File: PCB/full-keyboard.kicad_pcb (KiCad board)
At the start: 2 copper layers, 332 parts, among them J1 Conn_01x04_Pin, SW1 SW_Push, SW10 SW_Push, SW100 SW_Push, SW101 SW_Push, SW102 SW_Push, SW103 SW_Push, SW104 SW_Push, SW105 SW_Push, SW106 SW_Push, SW107 SW_Push, SW108 SW_Push, SW109 RotaryEncoder_Switch, SW11 SW_Push, SW110 RotaryEncoder_Switch, SW12 SW_Push, SW13 SW_Push, SW14 SW_Push, SW15 SW_Push, SW16 SW_Push, SW17 SW_Push, SW18 SW_Push, SW19 SW_Push, SW2 SW_Push, SW20 SW_Push, SW21 SW_Push, SW22 SW_Push, SW23 SW_Push, SW24 SW_Push, SW25 SW_Push, SW26 SW_Push, SW27 SW_Push, SW28 SW_Push, SW29 SW_Push, SW3 SW_Push, SW30 SW_Push, SW31 SW_Push, SW32 SW_Push, SW33 SW_Push, SW34 SW_Push, SW35 SW_Push, SW36 SW_Push, SW37 SW_Push, SW38 SW_Push, SW39 SW_Push, SW4 SW_Push, SW40 SW_Push, SW41 SW_Push, SW42 SW_Push, SW43 SW_Push, SW44 SW_Push, SW45 SW_Push, SW46 SW_Push, SW47 SW_Push, SW48 SW_Push, SW49 SW_Push, SW5 SW_Push, SW50 SW_Push, SW51 SW_Push, SW52 SW_Push, SW53 SW_Push, SW54 SW_Push, SW55 SW_Push, SW56 SW_Push, SW57 SW_Push, SW58 SW_Push, SW59 SW_Push, SW6 SW_Push, SW60 SW_Push, SW61 SW_Push, SW62 SW_Push, SW63 SW_Push, SW64 SW_Push, SW65 SW_Push, SW66 SW_Push, SW67 SW_Push, SW68 SW_Push, SW69 SW_Push, SW7 SW_Push, SW70 SW_Push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

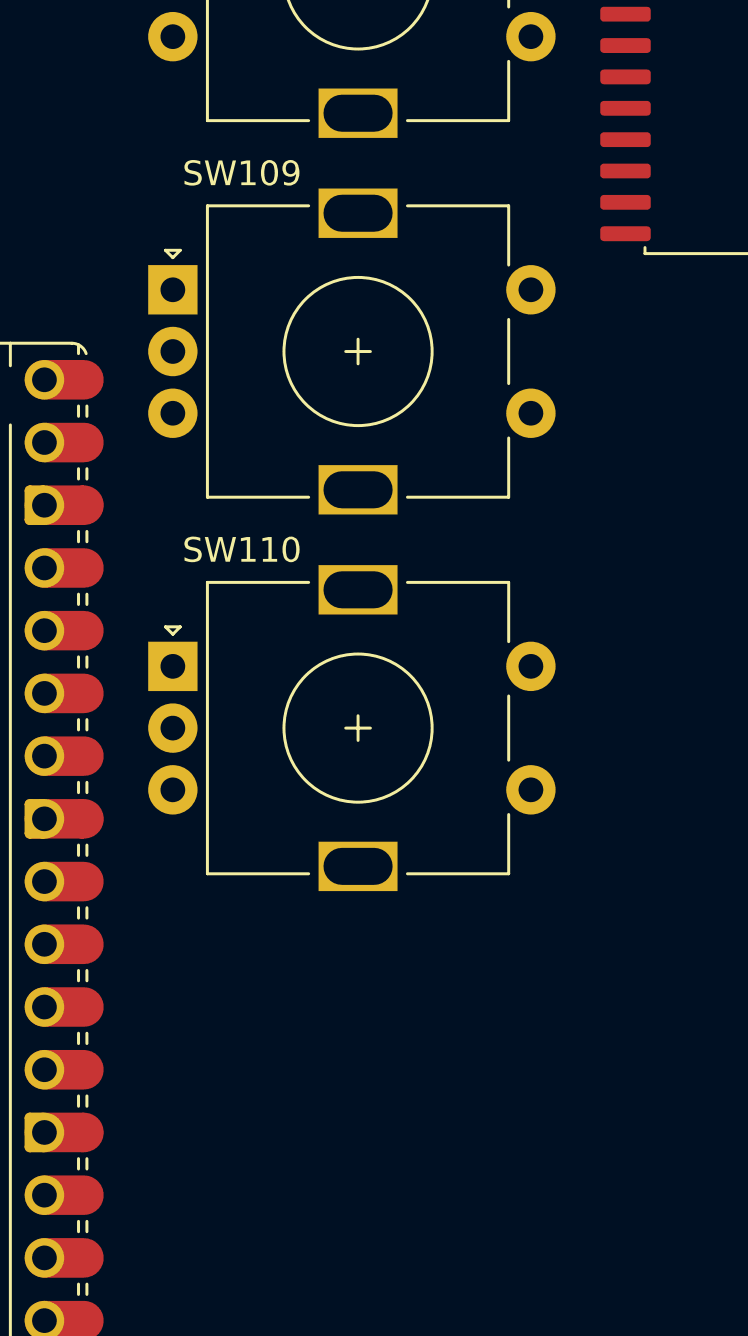
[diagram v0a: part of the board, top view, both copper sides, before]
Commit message: updated some footprints and found a cheaper hotswap socket kit
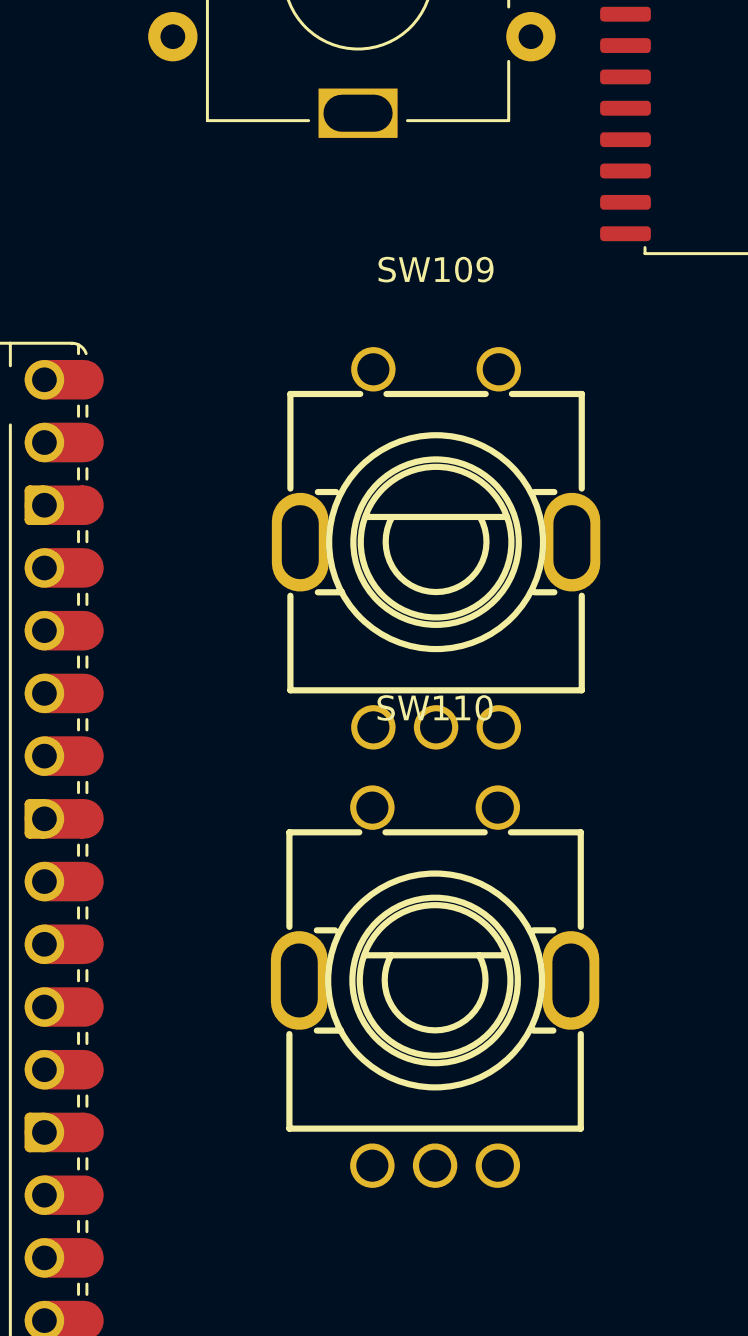
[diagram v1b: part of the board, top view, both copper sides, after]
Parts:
- SW109, SW110: footprint Rotary_Encoder:RotaryEncoder_Alps_EC11E-Switch_Vertical_H20mm -> easyeda2kicad:SW-TH_EC11XXXXXXXX
- moved SW110 16.8 mm to (504.5, 187.5)
- moved SW109 14.9 mm to (504.5, 169.8)

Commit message: worked on laying out the keyboard
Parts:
- R1, R2, R3: footprint easyeda2kicad:RES-TH_BD2.5-L4.7-P8.70-D0.5 -> Resistor_THT:R_Axial_DIN0207_L6.3mm_D2.5mm_P2.54mm_Vertical
- U1: footprint Package_SO:SOIC-28W_7.5x17.9mm_P1.27mm -> Package_DIP:DIP-28_W7.62mm
- moved SW1 272.0 mm to (46.6, 63.5)
- moved SW2 233.5 mm to (85.6, 63.5)
- moved SW3 215.5 mm to (105.6, 63.5)
- moved SW4 200.0 mm to (125.1, 63.5)
- moved SW104 190.8 mm to (525.8, 345.6)
- moved SW12 190.8 mm to (385.4, 433.4)
- moved SW19 190.8 mm to (402.9, 345.6)
- moved SW24 190.8 mm to (402.9, 433.4)
- moved SW31 190.8 mm to (420.5, 345.6)
- moved SW36 190.8 mm to (420.5, 433.4)
- moved SW43 190.8 mm to (438.0, 345.6)
- moved SW48 190.8 mm to (438.0, 433.4)
- moved SW55 190.8 mm to (455.6, 345.6)
- moved SW60 190.8 mm to (455.6, 433.4)
- moved SW67 190.8 mm to (473.1, 345.6)
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
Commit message: started laying out the pcb
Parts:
- moved SW12 379.5 mm to (302.0, 63.1)
- moved SW11 366.5 mm to (282.6, 64.0)
- moved SW10 356.4 mm to (263.1, 63.5)
- moved SW9 351.6 mm to (233.5, 63.6)
- moved SW8 345.1 mm to (214.0, 63.6)
- moved SW18 265.9 mm to (431.0, 63.6)
- moved SW17 247.1 mm to (411.1, 63.5)
- moved SW16 229.9 mm to (387.0, 63.6)
- moved SW15 214.9 mm to (367.0, 63.5)
- moved SW14 202.6 mm to (347.0, 63.1)
- moved SW13 194.1 mm to (322.5, 63.6)
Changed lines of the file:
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@@
 	(footprint "key-switches:SW_MX_Kailh_Choc_V1V2_THT_Hybrid"
 		(layer "F.Cu")
-		(at 385.38 363.15)
+		(at 214 63.65)
 		(descr "Compatible with Cherry MX, Kailh Choc V1 (PG1350) and Choc V2 (PG1353) mechanical keyboard switch, through-hole soldering, single-sided mounting.")
 		(tags "switch, low_profile")
@@
 	(footprint "key-switches:SW_MX_Kailh_Choc_V1V2_THT_Hybrid"
 		(layer "F.Cu")
-		(at 385.38 433.35)
+		(at 302 63.15)
 		(descr "Compatible with Cherry MX, Kailh Choc V1 (PG1350) and Choc V2 (PG1353) mechanical keyboard switch, through-hole soldering, single-sided mounting.")
 		(tags "switch, low_profile")
@@
 	(footprint "key-switches:SW_MX_Kailh_Choc_V1V2_THT_Hybrid"
 		(layer "F.Cu")
-		(at 385.38 415.8)
+		(at 282.58 64)
 		(descr "Compatible with Cherry MX, Kailh Choc V1 (PG1350) and Choc V2 (PG1353) mechanical keyboard switch, through-hole soldering, single-sided mounting.")
 		(tags "switch, low_profile")
@@
 	(footprint "key-switches:SW_MX_Kailh_Choc_V1V2_THT_Hybrid"
 		(layer "F.Cu")
-		(at 402.93 328.05)
+		(at 431 63.65)
 		(descr "Compatible with Cherry MX, Kailh Choc V1 (PG1350) and Choc V2 (PG1353) mechanical keyboard switch, through-hole soldering, single-sided mounting.")
 		(tags "switch, low_profile")
@@
 	(footprint "key-switches:SW_MX_Kailh_Choc_V1V2_THT_Hybrid"
 		(layer "F.Cu")
-		(at 402.93 257.85)
+		(at 347 63.15)
 		(descr "Compatible with Cherry MX, Kailh Choc V1 (PG1350) and Choc V2 (PG1353) mechanical keyboard switch, through-hole soldering, single-sided mounting.")
 		(tags "switch, low_profile")
@@
 	(footprint "key-switches:SW_MX_Kailh_Choc_V1V2_THT_Hybrid"
 		(layer "F.Cu")
-		(at 385.38 398.25)
+		(at 263.08 63.5)
 		(descr "Compatible with Cherry MX, Kailh Choc V1 (PG1350) and Choc V2 (PG1353) mechanical keyboard switch, through-hole soldering, single-sided mounting.")
 		(tags "switch, low_profile")
@@
 	(footprint "key-switches:SW_MX_Kailh_Choc_V1V2_THT_Hybrid"
 		(layer "F.Cu")
-		(at 385.38 380.7)
+		(at 233.5 63.65)
 		(descr "Compatible with Cherry MX, Kailh Choc V1 (PG1350) and Choc V2 (PG1353) mechanical keyboard switch, through-hole soldering, single-sided mounting.")
 		(tags "switch, low_profile")
@@
 	(footprint "key-switches:SW_MX_Kailh_Choc_V1V2_THT_Hybrid"
 		(layer "F.Cu")
-		(at 402.93 310.5)
+		(at 411.08 63.5)
 		(descr "Compatible with Cherry MX, Kailh Choc V1 (PG1350) and Choc V2 (PG1353) mechanical keyboard switch, through-hole soldering, single-sided mounting.")
 		(tags "switch, low_profile")
@@
 	(footprint "key-switches:SW_MX_Kailh_Choc_V1V2_THT_Hybrid"
 		(layer "F.Cu")
-		(at 402.93 240.3)
+		(at 322.5 63.65)
 		(descr "Compatible with Cherry MX, Kailh Choc V1 (PG1350) and Choc V2 (PG1353) mechanical keyboard switch, through-hole soldering, single-sided mounting.")
 		(tags "switch, low_profile")
@@
 	(footprint "key-switches:SW_MX_Kailh_Choc_V1V2_THT_Hybrid"
 		(layer "F.Cu")
-		(at 402.93 275.4)
+		(at 367 63.5)
 		(descr "Compatible with Cherry MX, Kailh Choc V1 (PG1350) and Choc V2 (PG1353) mechanical keyboard switch, through-hole soldering, single-sided mounting.")
 		(tags "switch, low_profile")
@@
 	(footprint "key-switches:SW_MX_Kailh_Choc_V1V2_THT_Hybrid"
 		(layer "F.Cu")
-		(at 402.93 292.95)
+		(at 387 63.65)
 		(descr "Compatible with Cherry MX, Kailh Choc V1 (PG1350) and Choc V2 (PG1353) mechanical keyboard switch, through-hole soldering, single-sided mounting.")
 		(tags "switch, low_profile")

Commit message: set the layout in the schematic to match the pcb layout for the keys
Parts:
- removed SW110: RotaryEncoder_Switch, easyeda2kicad:SW-TH_EC11XXXXXXXX
- SW95: footprint Rotary_Encoder:RotaryEncoder_Alps_EC11E-Switch_Vertical_H20mm -> key-switches:SW_MX_Kailh_Choc_V1V2_THT_Hybrid
- moved SW96 520.6 mm to (48.5, 171.5)
- moved SW97 506.8 mm to (74.0, 172.0)
- moved SW79 472.6 mm to (59.6, 152.0)
- moved SW21 458.1 mm to (46.5, 93.0)
- moved SW22 454.2 mm to (66.6, 93.0)
- moved SW23 452.7 mm to (85.6, 93.0)
- moved SW80 452.0 mm to (91.0, 152.2)
- moved SW24 451.9 mm to (105.6, 93.0)
- moved SW81 443.6 mm to (110.6, 152.0)
- moved SW63 442.8 mm to (54.0, 132.5)
- moved SW42 442.3 mm to (51.6, 113.0)
- moved SW82 436.7 mm to (130.1, 152.0)
- moved SW83 431.5 mm to (149.5, 151.7)
- moved SW98 431.3 mm to (100.0, 171.5)
- moved SW43 430.5 mm to (76.0, 112.7)
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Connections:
- D1 pad 1: /ROW0 -> unconnected-(D1-K-Pad1)
- D10 pad 1: /ROW0 -> unconnected-(D10-K-Pad1)
- D100 pad 1: /ROW5 -> unconnected-(D100-K-Pad1)
- D101 pad 1: /ROW5 -> unconnected-(D101-K-Pad1)
- D102 pad 1: /ROW5 -> unconnected-(D102-K-Pad1)
- D103 pad 1: /ROW5 -> unconnected-(D103-K-Pad1)
- D104 pad 1: /ROW5 -> unconnected-(D104-K-Pad1)
- D105 pad 1: /ROW5 -> unconnected-(D105-K-Pad1)
- D106 pad 1: /ROW5 -> unconnected-(D106-K-Pad1)
- D107 pad 1: /ROW5 -> unconnected-(D107-K-Pad1)
- D108 pad 1: /ROW5 -> unconnected-(D108-K-Pad1)
- D11 pad 1: /ROW0 -> unconnected-(D11-K-Pad1)
- D12 pad 1: /ROW0 -> unconnected-(D12-K-Pad1)
- D13 pad 1: /ROW0 -> unconnected-(D13-K-Pad1)
- D14 pad 1: /ROW0 -> unconnected-(D14-K-Pad1)
- D15 pad 1: /ROW0 -> unconnected-(D15-K-Pad1)
- D16 pad 1: /ROW0 -> unconnected-(D16-K-Pad1)
- D17 pad 1: /ROW0 -> unconnected-(D17-K-Pad1)
- D18 pad 1: /ROW0 -> unconnected-(D18-K-Pad1)
- D19 pad 1: /ROW1 -> unconnected-(D19-K-Pad1)
- D2 pad 1: /ROW0 -> unconnected-(D2-K-Pad1)
- D20 pad 1: /ROW1 -> unconnected-(D20-K-Pad1)
- D21 pad 1: /ROW1 -> unconnected-(D21-K-Pad1)
- D22 pad 1: /ROW1 -> unconnected-(D22-K-Pad1)
- D23 pad 1: /ROW1 -> unconnected-(D23-K-Pad1)
- D24 pad 1: /ROW1 -> unconnected-(D24-K-Pad1)
- D25 pad 1: /ROW1 -> unconnected-(D25-K-Pad1)
- D26 pad 1: /ROW1 -> unconnected-(D26-K-Pad1)
- D27 pad 1: /ROW1 -> unconnected-(D27-K-Pad1)
- D28 pad 1: /ROW1 -> unconnected-(D28-K-Pad1)
- D29 pad 1: /ROW1 -> unconnected-(D29-K-Pad1)
- D3 pad 1: /ROW0 -> unconnected-(D3-K-Pad1)
- D30 pad 1: /ROW1 -> unconnected-(D30-K-Pad1)
- D31 pad 1: /ROW1 -> unconnected-(D31-K-Pad1)
- D32 pad 1: /ROW1 -> unconnected-(D32-K-Pad1)
- D33 pad 1: /ROW1 -> unconnected-(D33-K-Pad1)
- D34 pad 1: /ROW1 -> unconnected-(D34-K-Pad1)
- D35 pad 1: /ROW1 -> unconnected-(D35-K-Pad1)
- D36 pad 1: /ROW1 -> unconnected-(D36-K-Pad1)
- D37 pad 1: /ROW2 -> unconnected-(D37-K-Pad1)
- D38 pad 1: /ROW2 -> unconnected-(D38-K-Pad1)
- D39 pad 1: /ROW2 -> unconnected-(D39-K-Pad1)
- D4 pad 1: /ROW0 -> unconnected-(D4-K-Pad1)
- D40 pad 1: /ROW2 -> unconnected-(D40-K-Pad1)
- D41 pad 1: /ROW2 -> unconnected-(D41-K-Pad1)
- D42 pad 1: /ROW2 -> unconnected-(D42-K-Pad1)
- D43 pad 1: /ROW2 -> unconnected-(D43-K-Pad1)
- D44 pad 1: /ROW2 -> unconnected-(D44-K-Pad1)
- D45 pad 1: /ROW2 -> unconnected-(D45-K-Pad1)
- D46 pad 1: /ROW2 -> unconnected-(D46-K-Pad1)
- D47 pad 1: /ROW2 -> unconnected-(D47-K-Pad1)
- D48 pad 1: /ROW2 -> unconnected-(D48-K-Pad1)
- D49 pad 1: /ROW2 -> unconnected-(D49-K-Pad1)
- D5 pad 1: /ROW0 -> unconnected-(D5-K-Pad1)
- D50 pad 1: /ROW2 -> unconnected-(D50-K-Pad1)
- D51 pad 1: /ROW2 -> unconnected-(D51-K-Pad1)
- D52 pad 1: /ROW2 -> unconnected-(D52-K-Pad1)
- D53 pad 1: /ROW2 -> unconnected-(D53-K-Pad1)
- D54 pad 1: /ROW2 -> unconnected-(D54-K-Pad1)
- D55 pad 1: /ROW3 -> unconnected-(D55-K-Pad1)
- D56 pad 1: /ROW3 -> unconnected-(D56-K-Pad1)
- D57 pad 1: /ROW3 -> unconnected-(D57-K-Pad1)
- D58 pad 1: /ROW3 -> unconnected-(D58-K-Pad1)
- D59 pad 1: /ROW3 -> unconnected-(D59-K-Pad1)
- D6 pad 1: /ROW0 -> unconnected-(D6-K-Pad1)
- D60 pad 1: /ROW3 -> unconnected-(D60-K-Pad1)
- D61 pad 1: /ROW3 -> unconnected-(D61-K-Pad1)
- D62 pad 1: /ROW3 -> unconnected-(D62-K-Pad1)
- D63 pad 1: /ROW3 -> unconnected-(D63-K-Pad1)
- D64 pad 1: /ROW3 -> unconnected-(D64-K-Pad1)
- D65 pad 1: /ROW3 -> unconnected-(D65-K-Pad1)
- D66 pad 1: /ROW3 -> unconnected-(D66-K-Pad1)
- D67 pad 1: /ROW3 -> unconnected-(D67-K-Pad1)
- D68 pad 1: /ROW3 -> unconnected-(D68-K-Pad1)
- D69 pad 1: /ROW3 -> unconnected-(D69-K-Pad1)
- D7 pad 1: /ROW0 -> unconnected-(D7-K-Pad1)
- D70 pad 1: /ROW3 -> unconnected-(D70-K-Pad1)
- D71 pad 1: /ROW3 -> unconnected-(D71-K-Pad1)
- D72 pad 1: /ROW3 -> unconnected-(D72-K-Pad1)
- D73 pad 1: /ROW4 -> unconnected-(D73-K-Pad1)
- D74 pad 1: /ROW4 -> unconnected-(D74-K-Pad1)
- D75 pad 1: /ROW4 -> unconnected-(D75-K-Pad1)
- D76 pad 1: /ROW4 -> unconnected-(D76-K-Pad1)
- D77 pad 1: /ROW4 -> unconnected-(D77-K-Pad1)
- D78 pad 1: /ROW4 -> unconnected-(D78-K-Pad1)
- D79 pad 1: /ROW4 -> unconnected-(D79-K-Pad1)
- D8 pad 1: /ROW0 -> unconnected-(D8-K-Pad1)
- D80 pad 1: /ROW4 -> unconnected-(D80-K-Pad1)
- D81 pad 1: /ROW4 -> unconnected-(D81-K-Pad1)
- D82 pad 1: /ROW4 -> unconnected-(D82-K-Pad1)
- D83 pad 1: /ROW4 -> unconnected-(D83-K-Pad1)
- D84 pad 1: /ROW4 -> unconnected-(D84-K-Pad1)
- D85 pad 1: /ROW4 -> unconnected-(D85-K-Pad1)
- D86 pad 1: /ROW4 -> unconnected-(D86-K-Pad1)
- D87 pad 1: /ROW4 -> unconnected-(D87-K-Pad1)
- D88 pad 1: /ROW4 -> unconnected-(D88-K-Pad1)
- D89 pad 1: /ROW4 -> unconnected-(D89-K-Pad1)
- D9 pad 1: /ROW0 -> unconnected-(D9-K-Pad1)
- D90 pad 1: /ROW4 -> unconnected-(D90-K-Pad1)
- D91 pad 1: /ROW5 -> unconnected-(D91-K-Pad1)
- D92 pad 1: /ROW5 -> unconnected-(D92-K-Pad1)
- D93 pad 1: /ROW5 -> unconnected-(D93-K-Pad1)
- D94 pad 1: /ROW5 -> unconnected-(D94-K-Pad1)
- D95 pad 1: /ROW5 -> unconnected-(D95-K-Pad1)
- D96 pad 1: /ROW5 -> unconnected-(D96-K-Pad1)
- D97 pad 1: /ROW5 -> unconnected-(D97-K-Pad1)
- D98 pad 1: /ROW5 -> unconnected-(D98-K-Pad1)
- D99 pad 1: /ROW5 -> unconnected-(D99-K-Pad1)
- SW1 pad 1: /COL0 -> unconnected-(SW1-Pad1)
- SW10 pad 1: /COL9 -> unconnected-(SW10-Pad1)
- SW100 pad 1: /COL9 -> unconnected-(SW100-Pad1)
- SW101 pad 1: /COL10 -> unconnected-(SW101-Pad1)
- SW102 pad 1: /COL11 -> unconnected-(SW102-Pad1)
- SW103 pad 1: /COL12 -> unconnected-(SW103-Pad1)
- SW104 pad 1: /COL13 -> unconnected-(SW104-Pad1)
- SW105 pad 1: /COL14 -> unconnected-(SW105-Pad1)
- SW106 pad 1: /COL15 -> unconnected-(SW106-Pad1)
- SW107 pad 1: /COL16 -> unconnected-(SW107-Pad1)
- SW108 pad 1: /COL17 -> unconnected-(SW108-Pad1)
- SW11 pad 1: /COL10 -> unconnected-(SW11-Pad1)
- SW12 pad 1: /COL11 -> unconnected-(SW12-Pad1)
- SW13 pad 1: /COL12 -> unconnected-(SW13-Pad1)
- SW14 pad 1: /COL13 -> unconnected-(SW14-Pad1)
- SW15 pad 1: /COL14 -> unconnected-(SW15-Pad1)
- SW16 pad 1: /COL15 -> unconnected-(SW16-Pad1)
- SW17 pad 1: /COL16 -> unconnected-(SW17-Pad1)
- SW18 pad 1: /COL17 -> unconnected-(SW18-Pad1)
- SW19 pad 1: /COL0 -> unconnected-(SW19-Pad1)
- SW2 pad 1: /COL1 -> unconnected-(SW2-Pad1)
- SW20 pad 1: /COL1 -> unconnected-(SW20-Pad1)
- SW21 pad 1: /COL2 -> unconnected-(SW21-Pad1)
- SW22 pad 1: /COL3 -> unconnected-(SW22-Pad1)
- SW23 pad 1: /COL4 -> unconnected-(SW23-Pad1)
- SW24 pad 1: /COL5 -> unconnected-(SW24-Pad1)
- SW25 pad 1: /COL6 -> unconnected-(SW25-Pad1)
- SW26 pad 1: /COL7 -> unconnected-(SW26-Pad1)
- SW27 pad 1: /COL8 -> unconnected-(SW27-Pad1)
- SW28 pad 1: /COL9 -> unconnected-(SW28-Pad1)
- SW29 pad 1: /COL10 -> unconnected-(SW29-Pad1)
- SW3 pad 1: /COL2 -> unconnected-(SW3-Pad1)
- SW30 pad 1: /COL11 -> unconnected-(SW30-Pad1)
- SW31 pad 1: /COL12 -> unconnected-(SW31-Pad1)
- SW32 pad 1: /COL13 -> unconnected-(SW32-Pad1)
- SW33 pad 1: /COL14 -> unconnected-(SW33-Pad1)
- SW34 pad 1: /COL15 -> unconnected-(SW34-Pad1)
- SW35 pad 1: /COL16 -> unconnected-(SW35-Pad1)
- SW36 pad 1: /COL17 -> unconnected-(SW36-Pad1)
- SW37 pad 1: /COL0 -> unconnected-(SW37-Pad1)
- SW38 pad 1: /COL1 -> unconnected-(SW38-Pad1)
- SW39 pad 1: /COL2 -> unconnected-(SW39-Pad1)
- SW4 pad 1: /COL3 -> unconnected-(SW4-Pad1)
- SW40 pad 1: /COL3 -> unconnected-(SW40-Pad1)
- SW41 pad 1: /COL4 -> unconnected-(SW41-Pad1)
- SW42 pad 1: /COL5 -> unconnected-(SW42-Pad1)
- SW43 pad 1: /COL6 -> unconnected-(SW43-Pad1)
- SW44 pad 1: /COL7 -> unconnected-(SW44-Pad1)
- SW45 pad 1: /COL8 -> unconnected-(SW45-Pad1)
- SW46 pad 1: /COL9 -> unconnected-(SW46-Pad1)
- SW47 pad 1: /COL10 -> unconnected-(SW47-Pad1)
- SW48 pad 1: /COL11 -> unconnected-(SW48-Pad1)
- SW49 pad 1: /COL12 -> unconnected-(SW49-Pad1)
- SW5 pad 1: /COL4 -> unconnected-(SW5-Pad1)
- SW50 pad 1: /COL13 -> unconnected-(SW50-Pad1)
- SW51 pad 1: /COL14 -> unconnected-(SW51-Pad1)
- SW52 pad 1: /COL15 -> unconnected-(SW52-Pad1)
- SW53 pad 1: /COL16 -> unconnected-(SW53-Pad1)
- SW54 pad 1: /COL17 -> unconnected-(SW54-Pad1)
- SW55 pad 1: /COL0 -> unconnected-(SW55-Pad1)
- SW56 pad 1: /COL1 -> unconnected-(SW56-Pad1)
- SW57 pad 1: /COL2 -> unconnected-(SW57-Pad1)
- SW58 pad 1: /COL3 -> unconnected-(SW58-Pad1)
- SW59 pad 1: /COL4 -> unconnected-(SW59-Pad1)
- SW6 pad 1: /COL5 -> unconnected-(SW6-Pad1)
- SW60 pad 1: /COL5 -> unconnected-(SW60-Pad1)
- SW61 pad 1: /COL6 -> unconnected-(SW61-Pad1)
- SW62 pad 1: /COL7 -> unconnected-(SW62-Pad1)
- SW63 pad 1: /COL8 -> unconnected-(SW63-Pad1)
- SW64 pad 1: /COL9 -> unconnected-(SW64-Pad1)
- SW65 pad 1: /COL10 -> unconnected-(SW65-Pad1)
- SW66 pad 1: /COL11 -> unconnected-(SW66-Pad1)
- SW67 pad 1: /COL12 -> unconnected-(SW67-Pad1)
- SW68 pad 1: /COL13 -> unconnected-(SW68-Pad1)
- SW69 pad 1: /COL14 -> unconnected-(SW69-Pad1)
- SW7 pad 1: /COL6 -> unconnected-(SW7-Pad1)
- SW70 pad 1: /COL15 -> unconnected-(SW70-Pad1)
- SW71 pad 1: /COL16 -> unconnected-(SW71-Pad1)
- SW72 pad 1: /COL17 -> unconnected-(SW72-Pad1)
- SW73 pad 1: /COL0 -> unconnected-(SW73-Pad1)
- SW74 pad 1: /COL1 -> unconnected-(SW74-Pad1)
- SW75 pad 1: /COL2 -> unconnected-(SW75-Pad1)
- SW76 pad 1: /COL3 -> unconnected-(SW76-Pad1)
- SW77 pad 1: /COL4 -> unconnected-(SW77-Pad1)
- SW78 pad 1: /COL5 -> unconnected-(SW78-Pad1)
- SW79 pad 1: /COL6 -> unconnected-(SW79-Pad1)
- SW8 pad 1: /COL7 -> unconnected-(SW8-Pad1)
- SW80 pad 1: /COL7 -> unconnected-(SW80-Pad1)
- SW81 pad 1: /COL8 -> unconnected-(SW81-Pad1)
- SW82 pad 1: /COL9 -> unconnected-(SW82-Pad1)
- SW83 pad 1: /COL10 -> unconnected-(SW83-Pad1)
- SW84 pad 1: /COL11 -> unconnected-(SW84-Pad1)
- SW85 pad 1: /COL12 -> unconnected-(SW85-Pad1)
- SW86 pad 1: /COL13 -> unconnected-(SW86-Pad1)
- SW87 pad 1: /COL14 -> unconnected-(SW87-Pad1)
- SW88 pad 1: /COL15 -> unconnected-(SW88-Pad1)
- SW89 pad 1: /COL16 -> unconnected-(SW89-Pad1)
- SW9 pad 1: /COL8 -> unconnected-(SW9-Pad1)
- SW90 pad 1: /COL17 -> unconnected-(SW90-Pad1)
- SW91 pad 1: /COL0 -> unconnected-(SW91-Pad1)
- SW92 pad 1: /COL1 -> unconnected-(SW92-Pad1)
- SW93 pad 1: /COL2 -> unconnected-(SW93-Pad1)
- SW94 pad 1: /COL3 -> unconnected-(SW94-Pad1)
- SW96 pad 1: /COL5 -> unconnected-(SW96-Pad1)
- SW97 pad 1: /COL6 -> unconnected-(SW97-Pad1)
- SW98 pad 1: /COL7 -> unconnected-(SW98-Pad1)
- SW99 pad 1: /COL8 -> unconnected-(SW99-Pad1)
- U1 pad 3: /RotEncoder2A -> unconnected-(U1-GPB2-Pad3)
- U1 pad 4: /RotEncoder2B -> unconnected-(U1-GPB3-Pad4)

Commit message: changed the key matrix and started swapping keyswith libraries
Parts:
- added SW110: RotaryEncoder_Switch, easyeda2kicad:SW-TH_EC11XXXXXXXX, F.Cu at (304.0, 247.2)
- D109: moved to B.Cu
- SW1, SW10, SW104, SW105, SW106, SW108, SW11, SW12, SW13, SW14, SW15, SW16, SW17, SW18, SW19, SW2, SW20, SW21, SW22, SW23, SW24, SW25, SW26, SW27, SW28, SW29, SW3, SW30, SW31, SW32, SW33, SW34, SW35, SW36, SW37, SW38, SW39, SW4, SW40, SW41, SW43, SW44, SW45, SW46, SW47, SW48, SW49, SW5, SW50, SW51, SW52, SW53, SW54, SW55, SW56, SW57, SW58, SW59, SW6, SW60, SW61, SW62, SW64, SW65, SW66, SW67, SW68, SW69, SW7, SW70, SW71, SW72, SW73, SW74, SW75, SW76, SW77, SW78, SW8, SW80, SW81, SW82, SW83, SW84, SW85, SW86, SW87, SW88, SW89, SW9, SW90, SW91, SW92, SW93, SW94, SW99: footprint key-switches:SW_MX_Kailh_Choc_V1V2_THT_Hybrid -> PCM_Switch_Keyboard_Hotswap_Kailh:SW_Hotswap_Kailh_MX_1.00u
- SW100, SW101, SW102, SW103, SW96, SW97, SW98: footprint key-switches:SW_MX_Kailh_Choc_V1V2_THT_Hybrid -> CherryMX_PCB_KailhSocket_LED:CherryMX_1.25u_PCB_KailhSocket_LED
- SW107: footprint key-switches:SW_MX_Kailh_Choc_V1V2_THT_Hybrid -> CherryMX_KailhSocket_StabWireTop_LTST-A683CEGBW-Rotated-HS:CherryMX_2.00u_KailhSocket_StabWireTop_LTST-A683CEGBW-Rotate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
- SW42: footprint key-switches:SW_MX_Kailh_Choc_V1V2_THT_Hybrid -> CherryMX_PCB_KailhSocket_LED:CherryMX_1.50u_PCB_KailhSocket_LED
- SW63: footprint key-switches:SW_MX_Kailh_Choc_V1V2_THT_Hybrid -> CherryMX_PCB_KailhSocket_LED:CherryMX_1.75u_PCB_KailhSocket_LED
- SW79: footprint key-switches:SW_MX_Kailh_Choc_V1V2_THT_Hybrid -> CherryMX_PCB_KailhSocket_LED:CherryMX_2.25u_PCB_KailhSocket_LED
- SW95: footprint key-switches:SW_MX_Kailh_Choc_V1V2_THT_Hybrid -> PCM_Switch_Keyboard_Hotswap_Kailh:SW_Hotswap_Kailh_MX_2.00u_90deg
- moved D109 519.5 mm to (46.5, 68.5), turned to 180 degrees
- moved D213 434.5 mm to (169.6, 214.7), turned to 90 degrees
- moved D214 428.2 mm to (176.2, 214.7), turned to 90 degrees
- moved D200 426.1 mm to (169.6, 222.8), turned to 90 degrees
- moved D215 422.1 mm to (182.8, 214.7), turned to 90 degrees
- moved D201 419.7 mm to (176.2, 222.8), turned to 90 degrees
- moved D187 417.8 mm to (169.6, 230.9), turned to 90 degrees
- moved D216 416.1 mm to (189.4, 214.7), turned to 90 degrees
- moved D202 413.4 mm to (182.8, 222.8), turned to 90 degrees
- moved D188 411.3 mm to (176.2, 230.9), turned to 90 degrees
- moved D174 409.7 mm to (169.6, 239.1), turned to 90 degrees
- moved D203 407.3 mm to (189.4, 222.8), turned to 90 degrees
- moved D189 404.9 mm to (182.8, 230.9), turned to 90 degrees
- moved D175 403.0 mm to (176.2, 239.1), turned to 90 degrees
- moved D161 401.7 mm to (169.6, 247.2), turned to 90 degrees
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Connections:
- A1 pad 25: /ROW0 -> /COL18
- A1 pad 26: /ROW1 -> /ROW0
- A1 pad 27: /ROW2 -> /ROW1
- A1 pad 29: /ROW3 -> /ROW2
- A1 pad 31: /ROW4 -> /ROW3
- A1 pad 32: /ROW5 -> /ROW4
- A1 pad 34: unconnected-(A1-GPIO28_ADC2-Pad34) -> /ROW5
- D1 pad 1: unconnected-(D1-K-Pad1) -> /ROW0
- D10 pad 1: unconnected-(D10-K-Pad1) -> /ROW0
- D100 pad 1: unconnected-(D100-K-Pad1) -> /ROW5
- D101 pad 1: unconnected-(D101-K-Pad1) -> /ROW5
- D102 pad 1: unconnected-(D102-K-Pad1) -> /ROW5
- D103 pad 1: unconnected-(D103-K-Pad1) -> /ROW5
- D104 pad 1: unconnected-(D104-K-Pad1) -> /ROW5
- D105 pad 1: unconnected-(D105-K-Pad1) -> /ROW5
- D106 pad 1: unconnected-(D106-K-Pad1) -> /ROW5
- D107 pad 1: unconnected-(D107-K-Pad1) -> /ROW5
- D108 pad 1: unconnected-(D108-K-Pad1) -> /ROW5
- D11 pad 1: unconnected-(D11-K-Pad1) -> /ROW0
- D12 pad 1: unconnected-(D12-K-Pad1) -> /ROW0
- D13 pad 1: unconnected-(D13-K-Pad1) -> /ROW0
- D14 pad 1: unconnected-(D14-K-Pad1) -> /ROW0
- D15 pad 1: unconnected-(D15-K-Pad1) -> /ROW0
- D16 pad 1: unconnected-(D16-K-Pad1) -> /ROW0
- D17 pad 1: unconnected-(D17-K-Pad1) -> /ROW0
- D18 pad 1: unconnected-(D18-K-Pad1) -> /ROW0
- D19 pad 1: unconnected-(D19-K-Pad1) -> /ROW0
- D2 pad 1: unconnected-(D2-K-Pad1) -> /ROW0
- D20 pad 1: unconnected-(D20-K-Pad1) -> /ROW1
- D21 pad 1: unconnected-(D21-K-Pad1) -> /ROW1
- D22 pad 1: unconnected-(D22-K-Pad1) -> /ROW1
- D23 pad 1: unconnected-(D23-K-Pad1) -> /ROW1
- D24 pad 1: unconnected-(D24-K-Pad1) -> /ROW1
- D25 pad 1: unconnected-(D25-K-Pad1) -> /ROW1
- D26 pad 1: unconnected-(D26-K-Pad1) -> /ROW1
- D27 pad 1: unconnected-(D27-K-Pad1) -> /ROW1
- D28 pad 1: unconnected-(D28-K-Pad1) -> /ROW1
- D29 pad 1: unconnected-(D29-K-Pad1) -> /ROW1
- D3 pad 1: unconnected-(D3-K-Pad1) -> /ROW0
- D30 pad 1: unconnected-(D30-K-Pad1) -> /ROW1
- D31 pad 1: unconnected-(D31-K-Pad1) -> /ROW1
- D32 pad 1: unconnected-(D32-K-Pad1) -> /ROW1
- D33 pad 1: unconnected-(D33-K-Pad1) -> /ROW1
- D34 pad 1: unconnected-(D34-K-Pad1) -> /ROW1
- D35 pad 1: unconnected-(D35-K-Pad1) -> /ROW1
- D36 pad 1: unconnected-(D36-K-Pad1) -> /ROW1
- D37 pad 1: unconnected-(D37-K-Pad1) -> /ROW1
- D38 pad 1: unconnected-(D38-K-Pad1) -> /ROW1
- D39 pad 1: unconnected-(D39-K-Pad1) -> /ROW2
- D4 pad 1: unconnected-(D4-K-Pad1) -> /ROW0
- D40 pad 1: unconnected-(D40-K-Pad1) -> /ROW2
- D41 pad 1: unconnected-(D41-K-Pad1) -> /ROW2
- D42 pad 1: unconnected-(D42-K-Pad1) -> /ROW2
- D43 pad 1: unconnected-(D43-K-Pad1) -> /ROW2
- D44 pad 1: unconnected-(D44-K-Pad1) -> /ROW2
- D45 pad 1: unconnected-(D45-K-Pad1) -> /ROW2
- D46 pad 1: unconnected-(D46-K-Pad1) -> /ROW2
- D47 pad 1: unconnected-(D47-K-Pad1) -> /ROW2
- D48 pad 1: unconnected-(D48-K-Pad1) -> /ROW2
- D49 pad 1: unconnected-(D49-K-Pad1) -> /ROW2
- D5 pad 1: unconnected-(D5-K-Pad1) -> /ROW0
- D50 pad 1: unconnected-(D50-K-Pad1) -> /ROW2
- D51 pad 1: unconnected-(D51-K-Pad1) -> /ROW2
- D52 pad 1: unconnected-(D52-K-Pad1) -> /ROW2
- D53 pad 1: unconnected-(D53-K-Pad1) -> /ROW2
- D54 pad 1: unconnected-(D54-K-Pad1) -> /ROW2
- D55 pad 1: unconnected-(D55-K-Pad1) -> /ROW2
- D56 pad 1: unconnected-(D56-K-Pad1) -> /ROW2
- D57 pad 1: unconnected-(D57-K-Pad1) -> /ROW2
- D58 pad 1: unconnected-(D58-K-Pad1) -> /ROW3
- D59 pad 1: unconnected-(D59-K-Pad1) -> /ROW3
- D6 pad 1: unconnected-(D6-K-Pad1) -> /ROW0
- D60 pad 1: unconnected-(D60-K-Pad1) -> /ROW3
- D61 pad 1: unconnected-(D61-K-Pad1) -> /ROW3
- D62 pad 1: unconnected-(D62-K-Pad1) -> /ROW3
- D63 pad 1: unconnected-(D63-K-Pad1) -> /ROW3
- D64 pad 1: unconnected-(D64-K-Pad1) -> /ROW3
- D65 pad 1: unconnected-(D65-K-Pad1) -> /ROW3
- D66 pad 1: unconnected-(D66-K-Pad1) -> /ROW3
- D67 pad 1: unconnected-(D67-K-Pad1) -> /ROW3
- D68 pad 1: unconnected-(D68-K-Pad1) -> /ROW3
- D69 pad 1: unconnected-(D69-K-Pad1) -> /ROW3
- D7 pad 1: unconnected-(D7-K-Pad1) -> /ROW0
- D70 pad 1: unconnected-(D70-K-Pad1) -> /ROW3
- D71 pad 1: unconnected-(D71-K-Pad1) -> /ROW3
- D72 pad 1: unconnected-(D72-K-Pad1) -> /ROW3
- D73 pad 1: unconnected-(D73-K-Pad1) -> /ROW3
- D74 pad 1: unconnected-(D74-K-Pad1) -> /ROW3
- D75 pad 1: unconnected-(D75-K-Pad1) -> /ROW3
- D76 pad 1: unconnected-(D76-K-Pad1) -> /ROW3
- D77 pad 1: unconnected-(D77-K-Pad1) -> /ROW4
- D78 pad 1: unconnected-(D78-K-Pad1) -> /ROW4
- D79 pad 1: unconnected-(D79-K-Pad1) -> /ROW4
- D8 pad 1: unconnected-(D8-K-Pad1) -> /ROW0
- D80 pad 1: unconnected-(D80-K-Pad1) -> /ROW4
- D81 pad 1: unconnected-(D81-K-Pad1) -> /ROW4
- D82 pad 1: unconnected-(D82-K-Pad1) -> /ROW4
- D83 pad 1: unconnected-(D83-K-Pad1) -> /ROW4
- D84 pad 1: unconnected-(D84-K-Pad1) -> /ROW4
- D85 pad 1: unconnected-(D85-K-Pad1) -> /ROW4
- D86 pad 1: unconnected-(D86-K-Pad1) -> /ROW4
- D87 pad 1: unconnected-(D87-K-Pad1) -> /ROW4
- D88 pad 1: unconnected-(D88-K-Pad1) -> /ROW4
- D89 pad 1: unconnected-(D89-K-Pad1) -> /ROW4
- D9 pad 1: unconnected-(D9-K-Pad1) -> /ROW0
- D90 pad 1: unconnected-(D90-K-Pad1) -> /ROW4
- D91 pad 1: unconnected-(D91-K-Pad1) -> /ROW4
- D92 pad 1: unconnected-(D92-K-Pad1) -> /ROW4
- D93 pad 1: unconnected-(D93-K-Pad1) -> /ROW4
- D94 pad 1: unconnected-(D94-K-Pad1) -> /ROW4
- D95 pad 1: unconnected-(D95-K-Pad1) -> /ROW4
- D96 pad 1: unconnected-(D96-K-Pad1) -> /ROW5
- D97 pad 1: unconnected-(D97-K-Pad1) -> /ROW5
- D98 pad 1: unconnected-(D98-K-Pad1) -> /ROW5
- D99 pad 1: unconnected-(D99-K-Pad1) -> /ROW5
- SW1 pad 1: unconnected-(SW1-Pad1) -> /COL0
- SW10 pad 1: unconnected-(SW10-Pad1) -> /COL9
- SW100 pad 1: unconnected-(SW100-Pad1) -> /COL9
- SW101 pad 1: unconnected-(SW101-Pad1) -> /COL10
- SW102 pad 1: unconnected-(SW102-Pad1) -> /COL11
- SW103 pad 1: unconnected-(SW103-Pad1) -> /COL12
- SW104 pad 1: unconnected-(SW104-Pad1) -> /COL14
- SW105 pad 1: unconnected-(SW105-Pad1) -> /COL15
- SW106 pad 1: unconnected-(SW106-Pad1) -> /COL16
- SW107 pad 1: unconnected-(SW107-Pad1) -> /COL17
- SW108 pad 1: unconnected-(SW108-Pad1) -> /COL18
- SW11 pad 1: unconnected-(SW11-Pad1) -> /COL10
- SW12 pad 1: unconnected-(SW12-Pad1) -> /COL11
- SW13 pad 1: unconnected-(SW13-Pad1) -> /COL12
- SW14 pad 1: unconnected-(SW14-Pad1) -> /COL13
- SW15 pad 1: unconnected-(SW15-Pad1) -> /COL14
- SW16 pad 1: unconnected-(SW16-Pad1) -> /COL15
- SW17 pad 1: unconnected-(SW17-Pad1) -> /COL16
- SW18 pad 1: unconnected-(SW18-Pad1) -> /COL17
- SW19 pad 1: unconnected-(SW19-Pad1) -> /COL18
- SW2 pad 1: unconnected-(SW2-Pad1) -> /COL1
- SW20 pad 1: unconnected-(SW20-Pad1) -> /COL0
- SW21 pad 1: unconnected-(SW21-Pad1) -> /COL1
- SW22 pad 1: unconnected-(SW22-Pad1) -> /COL2
- SW23 pad 1: unconnected-(SW23-Pad1) -> /COL3
- SW24 pad 1: unconnected-(SW24-Pad1) -> /COL4
- SW25 pad 1: unconnected-(SW25-Pad1) -> /COL5
- SW26 pad 1: unconnected-(SW26-Pad1) -> /COL6
- SW27 pad 1: unconnected-(SW27-Pad1) -> /COL7
- SW28 pad 1: unconnected-(SW28-Pad1) -> /COL8
- SW29 pad 1: unconnected-(SW29-Pad1) -> /COL9
- SW3 pad 1: unconnected-(SW3-Pad1) -> /COL2
- SW30 pad 1: unconnected-(SW30-Pad1) -> /COL10
- SW31 pad 1: unconnected-(SW31-Pad1) -> /COL11
- SW32 pad 1: unconnected-(SW32-Pad1) -> /COL12
- SW33 pad 1: unconnected-(SW33-Pad1) -> /COL13
- SW34 pad 1: unconnected-(SW34-Pad1) -> /COL14
- SW35 pad 1: unconnected-(SW35-Pad1) -> /COL15
- SW36 pad 1: unconnected-(SW36-Pad1) -> /COL16
- SW37 pad 1: unconnected-(SW37-Pad1) -> /COL17
- SW38 pad 1: unconnected-(SW38-Pad1) -> /COL18
- SW39 pad 1: unconnected-(SW39-Pad1) -> /COL0
- SW4 pad 1: unconnected-(SW4-Pad1) -> /COL3
- SW40 pad 1: unconnected-(SW40-Pad1) -> /COL1
- SW41 pad 1: unconnected-(SW41-Pad1) -> /COL2
- SW42 pad 1: unconnected-(SW42-Pad1) -> /COL3
- SW43 pad 1: unconnected-(SW43-Pad1) -> /COL4
- SW44 pad 1: unconnected-(SW44-Pad1) -> /COL5
- SW45 pad 1: unconnected-(SW45-Pad1) -> /COL6
- SW46 pad 1: unconnected-(SW46-Pad1) -> /COL7
- SW47 pad 1: unconnected-(SW47-Pad1) -> /COL8
- SW48 pad 1: unconnected-(SW48-Pad1) -> /COL9
- SW49 pad 1: unconnected-(SW49-Pad1) -> /COL10
- SW5 pad 1: unconnected-(SW5-Pad1) -> /COL4
- SW50 pad 1: unconnected-(SW50-Pad1) -> /COL11
- SW51 pad 1: unconnected-(SW51-Pad1) -> /COL12
- SW52 pad 1: unconnected-(SW52-Pad1) -> /COL13
- SW53 pad 1: unconnected-(SW53-Pad1) -> /COL14
- SW54 pad 1: unconnected-(SW54-Pad1) -> /COL15
- SW55 pad 1: unconnected-(SW55-Pad1) -> /COL16
- SW56 pad 1: unconnected-(SW56-Pad1) -> /COL17
- SW57 pad 1: unconnected-(SW57-Pad1) -> /COL18
- SW58 pad 1: unconnected-(SW58-Pad1) -> /COL0
- SW59 pad 1: unconnected-(SW59-Pad1) -> /COL1
- SW6 pad 1: unconnected-(SW6-Pad1) -> /COL5
- SW60 pad 1: unconnected-(SW60-Pad1) -> /COL2
- SW61 pad 1: unconnected-(SW61-Pad1) -> /COL3
- SW62 pad 1: unconnected-(SW62-Pad1) -> /COL4
- SW63 pad 1: unconnected-(SW63-Pad1) -> /COL5
- SW64 pad 1: unconnected-(SW64-Pad1) -> /COL6
- SW65 pad 1: unconnected-(SW65-Pad1) -> /COL7
- SW66 pad 1: unconnected-(SW66-Pad1) -> /COL8
- SW67 pad 1: unconnected-(SW67-Pad1) -> /COL9
- SW68 pad 1: unconnected-(SW68-Pad1) -> /COL10
- SW69 pad 1: unconnected-(SW69-Pad1) -> /COL11
- SW7 pad 1: unconnected-(SW7-Pad1) -> /COL6
- SW70 pad 1: unconnected-(SW70-Pad1) -> /COL12
- SW71 pad 1: unconnected-(SW71-Pad1) -> /COL13
- SW72 pad 1: unconnected-(SW72-Pad1) -> /COL14
- SW73 pad 1: unconnected-(SW73-Pad1) -> /COL15
- SW74 pad 1: unconnected-(SW74-Pad1) -> /COL16
- SW75 pad 1: unconnected-(SW75-Pad1) -> /COL17
- SW76 pad 1: unconnected-(SW76-Pad1) -> /COL18
- SW77 pad 1: unconnected-(SW77-Pad1) -> /COL0
- SW78 pad 1: unconnected-(SW78-Pad1) -> /COL1
- SW79 pad 1: unconnected-(SW79-Pad1) -> /COL2
- SW8 pad 1: unconnected-(SW8-Pad1) -> /COL7
- SW80 pad 1: unconnected-(SW80-Pad1) -> /COL3
- SW81 pad 1: unconnected-(SW81-Pad1) -> /COL4
- SW82 pad 1: unconnected-(SW82-Pad1) -> /COL5
- SW83 pad 1: unconnected-(SW83-Pad1) -> /COL6
- SW84 pad 1: unconnected-(SW84-Pad1) -> /COL7
- SW85 pad 1: unconnected-(SW85-Pad1) -> /COL8
- SW86 pad 1: unconnected-(SW86-Pad1) -> /COL9
- SW87 pad 1: unconnected-(SW87-Pad1) -> /COL10
- SW88 pad 1: unconnected-(SW88-Pad1) -> /COL11
- SW89 pad 1: unconnected-(SW89-Pad1) -> /COL12
- SW9 pad 1: unconnected-(SW9-Pad1) -> /COL8
- SW90 pad 1: unconnected-(SW90-Pad1) -> /COL13
- SW91 pad 1: unconnected-(SW91-Pad1) -> /COL14
- SW92 pad 1: unconnected-(SW92-Pad1) -> /COL15
- SW93 pad 1: unconnected-(SW93-Pad1) -> /COL16
- SW94 pad 1: unconnected-(SW94-Pad1) -> /COL17
- SW95 pad 1: unconnected-(SW95-Pad1) -> /COL18
- SW96 pad 1: unconnected-(SW96-Pad1) -> /COL1
- SW97 pad 1: unconnected-(SW97-Pad1) -> /COL2
- SW98 pad 1: unconnected-(SW98-Pad1) -> /COL3
- SW99 pad 1: unconnected-(SW99-Pad1) -> /COL6
- U1 pad 24: /RotEncoder2B1 -> unconnected-(U1-GPA3-Pad24)
- U1 pad 25: /RotEncoder2B2 -> unconnected-(U1-GPA4-Pad25)
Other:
- board outline added: 3.4 x 3 mm
